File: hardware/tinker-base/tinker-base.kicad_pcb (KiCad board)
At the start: 4 copper layers, 30.3 x 90.5 mm, 86 parts, among them J2 TYPE-C-31-M-12, J8 CON-SMA-EDGE-S, Q1 FS8205A, Q2 FS8205A, Q3 FS8205A, U1 W25Q128JVYIQ, U14 DW01A, U15 AANI-CH-0070, U16 E220-900MM22S, U22 TPS22918DBVR, U3 ESP32-S3RH2, U5 BQ21040DBVR, U9 TPS63020DSJR, Y1 ABS07-32.768KHZ-T, Y2 ECS-400-10-37B2-CKY-TR

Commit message: hardware(Tinker-Base): V1 design review and fixes -- the antenna window clear on every layer, 21 ground vias, L5/C25/fiducials, R52 1.2 k, and fab notes for the order
Stacked on #1545 (the Beetle/Mantis parts). The V1 JLC package was plotted from
exactly this board (md5 1fe1e414).

The review is new: hardware/tinker-base/design-review-2026-09-28.md. It has a
table of the fixes applied, and of the items left undone with the reason for each.

Layout (tinker-base.kicad_pcb):
- U15 antenna. F.Cu keeps the feed notch. A second rule area clears In1, In2 and
  B.Cu under the whole 4.6 x 3.0 mm window. Before this, In1 GND, In2 +3V3 and
  B.Cu GND filled under the feed pads. Nine GND fence vias.
- 21 GND vias: nine beside signal vias (signal vias more than 1 mm from a
  ground via: 14 -> 5), nine in U3's exposed pad between its paste windows, one
  for C16/C24 and two for U16's ground pads. Five old vias removed.
- J8 moved so its pads start 0.30 mm inside the edge. L5 (330 nH) runs from the
  SMA line to GND beside it.
- C25 (100 nF) on V_SWITCH at U9.
- J2's signal pads trimmed to HRO's land, in the library too. BT2.P to J2 goes
  from 0.40 to 0.84 mm.
- S3 gets an F.Cu keep-out over its body, and its GPIO0 via moves out from
  under it.
- Thermal reliefs on J2's shell legs and D6's cathode. Pin-1 dots on U3, U5, U22,
  CR1 and U16. FID1-FID3 added, R13/R16 refs hidden, and a B.Silk "-" at BT2's
  N end.
- Zones refilled. A second kicad-cli refill reproduces them byte for byte.

Schematic:
- L5, C25 and FID1-FID3 added.
- R52 680 -> 1.2 k. The charge current drops from 0.79 A to about 0.45 A, so the
  charger's heat no longer trips the board-mounted NTC from room temperature.
- Title blocks, rev V1, on all four sheets.
- bom.csv regenerated.

Library:
- IC_ESP32-S3 and 8L_WSON_8x6x3p4x4p3_MAC go back to their window polygons.
  4078070b had added paste pads on top of those polygons.
- USB_C_HRO_TYPE-C-31-M-12 pads trimmed.
- ANT_AANI-CH-0070_ABR's description states the r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
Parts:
- added C25: 100 nF, Capacitor_SMD:C_0402_1005Metric, F.Cu at (48.9, 171.8)
- added FID1: Fiducial, Fiducial:Fiducial_0.5mm_Mask1mm, F.Cu at (53.9, 108.1)
- added FID2: Fiducial, Fiducial:Fiducial_0.5mm_Mask1mm, F.Cu at (74.4, 121.6)
- added FID3: Fiducial, Fiducial:Fiducial_0.5mm_Mask1mm, F.Cu at (51.4, 187.6)
- added L5: 330 nH, Inductor_SMD:L_0603_1608Metric, F.Cu at (62.1, 108.8)
- R52: value 680 -> 1.2 k
- moved J8 1.14 mm to (62.9, 105.7)
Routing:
- net Net-(U3-GPIO0): track 14.2 -> 11.8 mm
- net GND: track 2.66 -> 3.69 mm, vias 184 -> 210

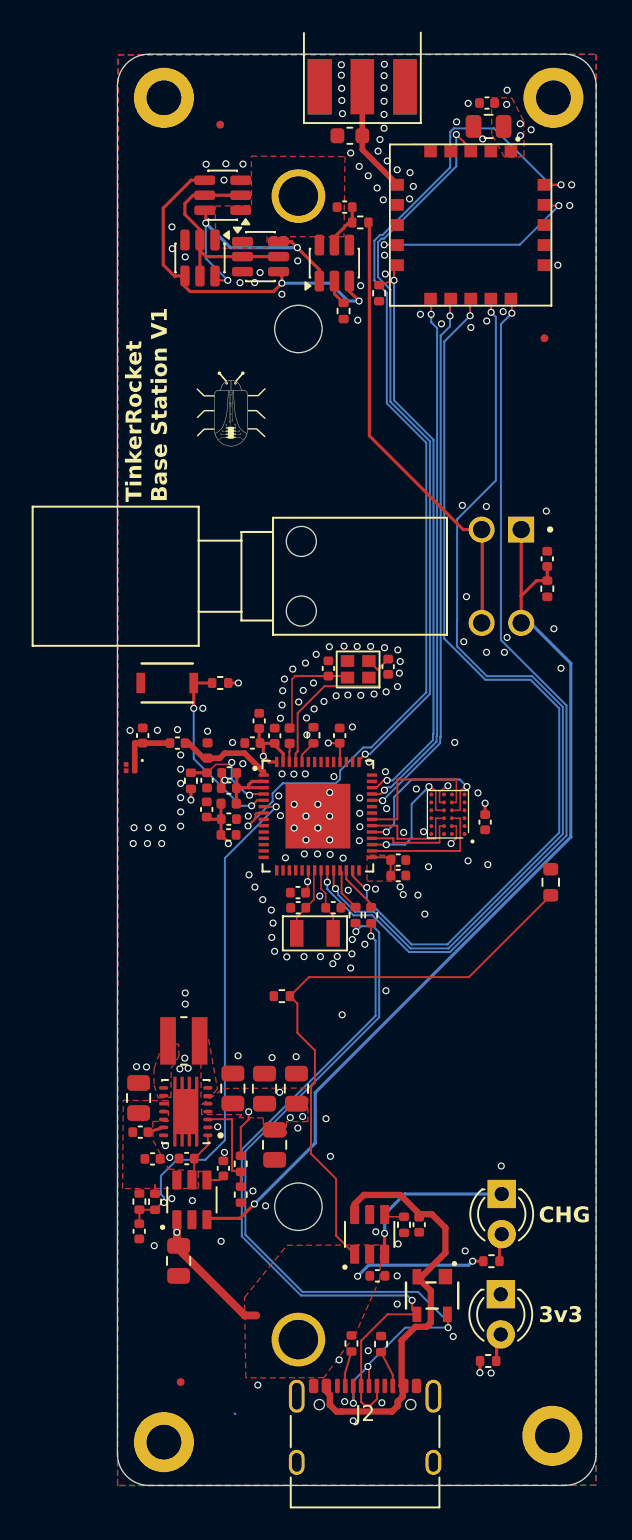
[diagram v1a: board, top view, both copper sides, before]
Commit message: hardware(Tinker-Base): three vias off their pads, and J2's rear fillets kept flat under BT2
Three vias had rings overlapping an SMD land. The first and third had their holes
at, or inside, the edge of the land's mask opening, so solder could wick down them.

- C16/C24 GND via, from (54.20, 149.55) to (53.52, 149.60). It sat in the 0.34 mm gap
  between C24.2 and C16.2. It now sits in the pocket between C8.1, C8.2, C24.2 and C16.2,
  with a 0.2 mm stub to the caps' strap, and serves C8.2 too. GPIO0's B.Cu diagonal,
  a static strap line, moves 0.5 mm down-right to free that pocket.
- U16 GND via, from (70.50, 109.00) on C20.1's edge to (70.97, 109.045). A 0.25 mm stub
  runs to U16 pad 2.
- U22 VCC via, from (51.16, 178.13) to (50.44, 178.25). It sat 0.19 mm below U22.1,
  inside that pad's 0.10 mm mask margin. It now sits beside the U22.1-C42.1 trace with a
  0.25 mm F.Cu stub. The In2 VCC track (µA) drops straight down to it.

Now no via ring touches any SMD mask opening except U3's nine thermal-pad vias. The
closest via hole is 0.10 mm from an opening, at C88.

BT2's flat base ends over the first 0.27 mm of J2's two rear shell-leg pads, which are
soldered from the bottom. The fab notes now say to keep those two fillets flat.

Checks:
- DRC (--severity-all --schematic-parity): 0 errors, the same 26 warnings, 0 unconnected,
  0 parity.
- The stored fills are a kicad-cli refill, and a second refill is byte-identical.
- check_board_parity: tinker-base 90/90.
- Signal vias more than 1 mm from a GND via: 5, unchanged.
- The U15 window is still clear. No footprint moved.

Co-Authored-By: Claude Opus 5.5 <noreply@anthropic.com>
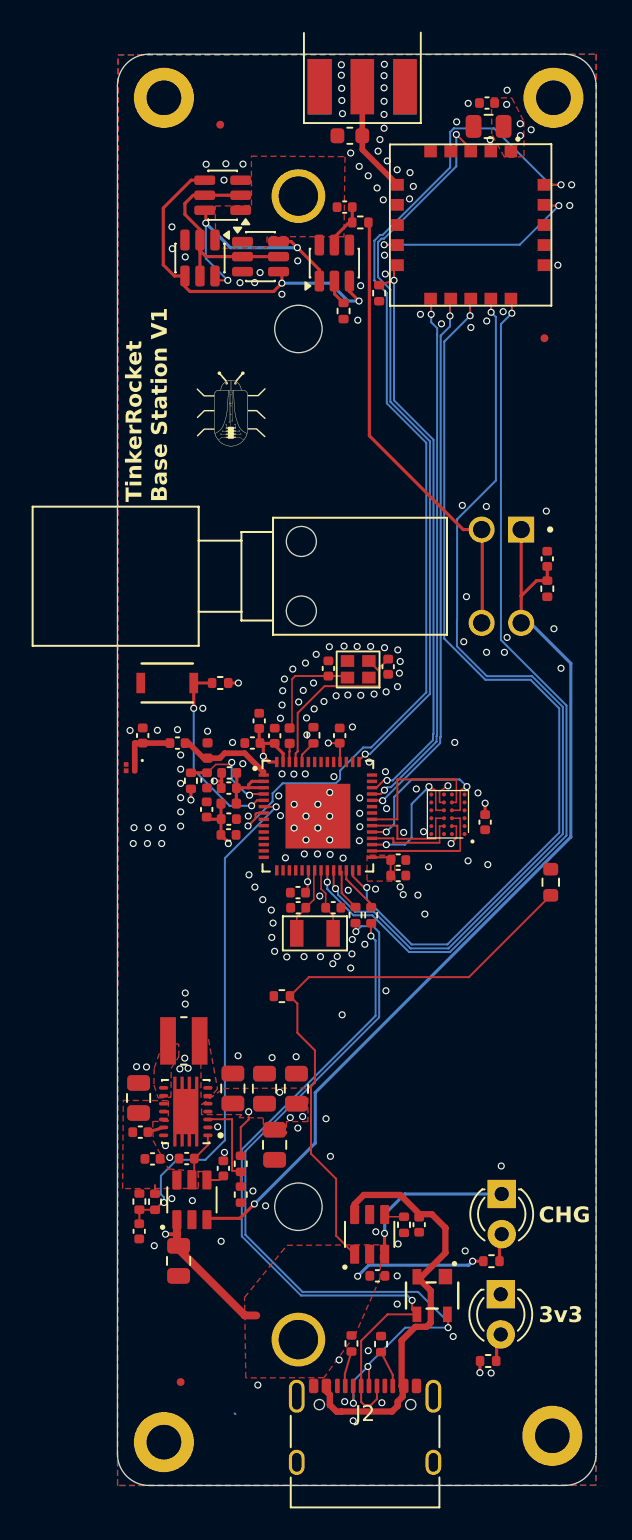
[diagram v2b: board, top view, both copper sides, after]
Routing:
- net GND: track 3.69 -> 4.91 mm
- net VCC: track 99.6 -> 100.1 mm
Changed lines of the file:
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@@
 	)
 	(segment
+		(start 70.97 109.045)
+		(end 71.01 109.79)
+		(width 0.25)
+		(layer "F.Cu")
+		(net "GND")
+	)
+	(segment
 		(start 60.53 142.06)
 		(end 60.52 142.05)
@@
 	)
 	(segment
-		(start 53.99 149.085)
+		(start 53.99 149.6)
 		(end 53.99 150.045)
 		(width 0.2)
@@
 		(net "GND")
 	)
+	(segment
+		(start 53.99 149.085)
+		(end 53.99 149.6)
+		(width 0.2)
+		(layer "F.Cu")
+		(net "GND")
+	)
+	(segment
+		(start 53.52 149.6)
+		(end 53.99 149.6)
+		(width 0.2)
+		(layer "F.Cu")
+		(net "GND")
+	)
 	(via
 		(at 65.5 152.85)
@@
 	)
 	(via
-		(at 54.2 149.55)
+		(at 53.52 149.6)
 		(size 0.45)
 		(drill 0.3)
@@
 	)
 	(via
-		(at 70.5 109)
+		(at 70.97 109.045)
 		(size 0.45)
 		(drill 0.3)
@@
 	)
 	(segment
-		(start 55.205 151.165)
+		(start 54.498 151.165)
 		(end 55.885 151.165)
 		(width 0.127)
@@
 	)
 	(segment
-		(start 52.226 148.186)
-		(end 55.205 151.165)
+		(start 52.226 148.893)
+		(end 54.498 151.165)
 		(width 0.127)
 		(layer "B.Cu")
@@
 	(segment
 		(start 52.226 145)
-		(end 52.226 148.186)
+		(end 52.226 148.893)
 		(width 0.127)
 		(layer "B.Cu")
@@
 	(segment
 		(start 51.16 177.335)
-		(end 51.16 178.13)
+		(end 51.16 178.25)
 		(width 0.5)
 		(layer "F.Cu")
@@
 	)
 	(segment
+		(start 50.44 178.25)
+		(end 51.16 178.25)
+		(width 0.25)
+		(layer "F.Cu")
+		(net "VCC")
+	)
+	(segment
 		(start 63.33 114.34)
 		(end 63.27 114.28)
@@
 	)
 	(segment
-		(start 51.16 178.13)
+		(start 51.16 178.25)
 		(end 51.16 178.62)
 		(width 0.5)
@@
 	)
 	(via
-		(at 51.16 178.13)
+		(at 50.44 178.25)
 		(size 0.45)
 		(drill 0.3)
@@
 	)
 	(segment
-		(start 51.16 178.13)
+		(start 50.44 178.25)
 		(end 50.44 177.41)
 		(width 0.5)

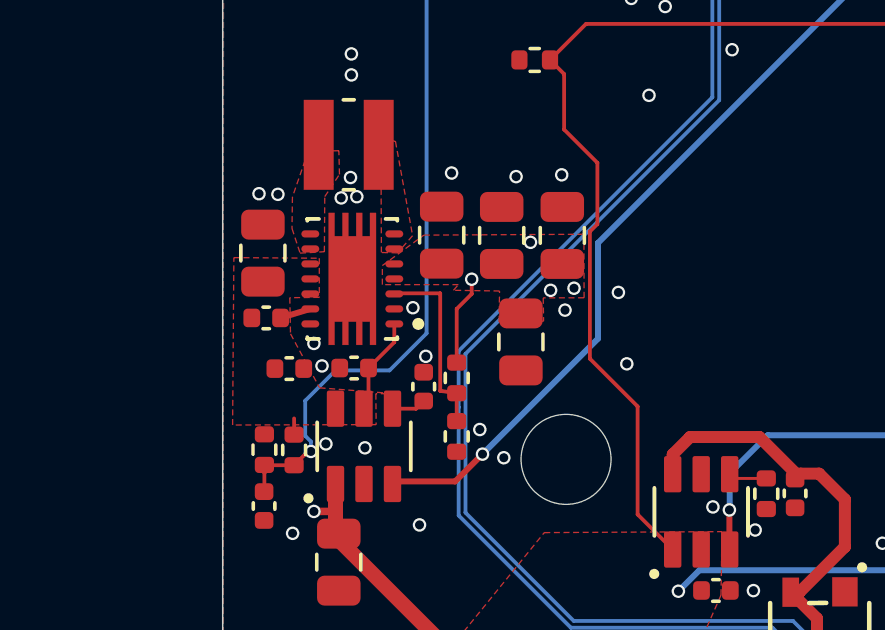
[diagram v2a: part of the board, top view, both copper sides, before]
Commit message: hardware(Tinker-Base): C26, 100 nF on U9's output beside VOUT, with FB running under it
Review item L8, output side, added at the owner's word. The 22 uF output caps'
ground pads return around the L2 switch-node pour, so the output had no short
high-frequency loop. C25 already fixes the same problem on the input side.

- C26: 100 nF, 0402, +3V3 to GND. It is drawn on the Power Switch sheet with
  #PWR0239/#PWR0240, and C23 was the template.
- Placement: (54.68, 171.48), rotated 180. The +3V3 pad sits on R13's +3V3 feed
  and on the output pour. That pour is the same top-layer copper as U9's VOUT
  pins and C58.
- FB: U9's FB line runs under the cap's body, between the pads, with 0.1265 mm
  and 0.1665 mm clearance. Its route is unchanged.
- Ground: U9 pin 2's GND via moves from (53.74, 171.46) to (53.77, 172.12), which
  C26's GND pad would otherwise have overlapped. A 0.25 mm link joins that pad to
  the via, which still serves pin 2 through the same top-layer ground.

Checks:
- DRC (--severity-all --schematic-parity): 0 errors, the same 26 warnings,
  0 unconnected, 0 parity.
- The stored fills are a kicad-cli refill, and a second refill is byte-identical.
- check_board_parity: tinker-base 91/91.
- ERC: 35 errors, unchanged.
- No via ring touches an SMD mask opening except U3's nine.
- The U15 window is still clear.
- bom.csv: C26 joins the 100 nF line, now 13. The generator reproduces the
  previous bom.csv exactly from the previous netlist.

Co-Authored-By: Claude Opus 5.5 <noreply@anthropic.com>
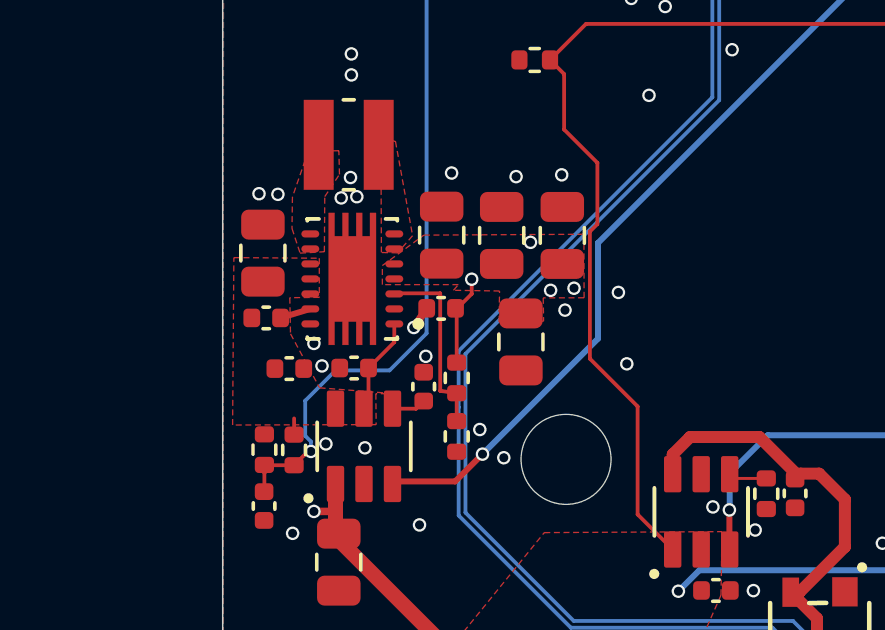
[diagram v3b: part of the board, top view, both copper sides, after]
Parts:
- added C26: 100 nF, Capacitor_SMD:C_0402_1005Metric, F.Cu at (54.7, 171.5)
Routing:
- net GND: track 4.91 -> 5.68 mm
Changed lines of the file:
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@@
+		)
+	)
+	(footprint "Capacitor_SMD:C_0402_1005Metric"
+		(layer "F.Cu")
+		(at 54.68 171.48 180)
+		(descr "Capacitor SMD 0402 (1005 Metric), square (rectangular) end terminal, IPC-7351 nominal, (Body size source: IPC-SM-782 page 76, https://www.pcb-3d.com/wordpress/wp-content/uploads/ipc-sm-782a_amendment_1_and_2.pdf)")
+		(tags "capacitor")
+		(property "Reference" "C26"
+			(at 0 -1.16 180)
+			(layer "F.SilkS")
+			(hide yes)
+			(effects
+				(font
+					(size 1 1)
+					(thickness 0.15)
+				)
+			)
+		)
+		(property "Value" "100 nF"
+			(at 0 1.16 180)
+			(layer "F.Fab")
+			(hide yes)
+			(effects
+				(font
+					(size 1 1)
+					(thickness 0.15)
+				)
+			)
+		)
+		(property "Datasheet" ""
+			(at 0 0 180)
+			(layer "F.Fab")
+			(hide yes)
+			(effects
+				(font
+					(size 1.27 1.27)
+				)
+			)
+		)
+		(property "Description" ""
+			(at 0 0 180)
+			(layer "F.Fab")
+			(hide yes)
+			(effects
+				(font
+					(size 1.27 1.27)
+				)
+			)
+		)
+		(property "KiLib_Generator" "SMD_2terminal_chip_molded"
+			(at 0 0 180)
+			(layer "F.SilkS")
+			(hide yes)
+			(effects
+				(font
+					(size 1 1)
+					(thickness 0.15)
+				)
+			)
+		)
+		(property "MPN" "CL05B104KO5NNNC"
+			(at 0 0 180)
+			(unlocked yes)
+			(layer "F.Fab")
+			(hide yes)
+			(effects
+				(font
+					(size 1 1)
+					(thickness 0.15)
+				)
+			)
+		)
+		(property "Mfr" "Samsung"
+			(at 0 0 180)
+			(unlocked yes)
+			(layer "F.Fab")
+			(hide yes)
+			(effects
+				(font
+					(size 1 1)
+					(thickness 0.15)
+				)
+			)
+		)
+		(sheetname "/Power Switch/")
+		(sheetfile "power.kicad_sch")
+		(attr smd)
+		(duplicate_pad_numbers_are_jumpers no)
+		(fp_line
+			(start -0.107836 0.36)
+			(end 0.107836 0.36)
+			(stroke
+				(width 0.12)
+				(type solid)
+			)
+			(layer "F.SilkS")
+		)
+		(fp_line
+			(start -0.107836 -0.36)
+			(end 0.107836 -0.36)
+			(stroke
+				(width 0.12)
+				(type solid)
+			)
+			(layer "F.SilkS")
+		)
+		(fp_rect
+			(start -0.91 -0.46)
+			(end 0.91 0.46)
+			(stroke
+				(width 0.05)
+				(type solid)
+			)
+			(fill no)
+			(layer "F.CrtYd")
+		)
+		(fp_rect
+			(start -0.5 -0.25)
+			(end 0.5 0.25)
+			(stroke
+				(width 0.1)
+				(type solid)
+			)
+			(fill no)
+			(layer "F.Fab")
+		)
+		(fp_text user "${REFERENCE}"
+			(at 0 0 0)
+			(layer "F.Fab")
+			(effects
+				(font
+					(size 0.25 0.25)
+					(thickness 0.04)
+				)
+			)
+		)
+		(pad "1" smd roundrect
+			(at -0.48 0 180)
+			(size 0.56 0.62)
+			(layers "F.Cu" "F.Mask" "F.Paste")
+			(roundrect_rratio 0.25)
+			(net "+3V3")
+			(pintype "passive")
+		)
+		(pad "2" smd roundrect
+			(at 0.48 0 180)
+			(size 0.56 0.62)
+			(layers "F.Cu" "F.Mask" "F.Paste")
+			(roundrect_rratio 0.25)
+			(net "GND")
+			(pintype "passive")
+		)
+		(embedded_fonts no)
+		(model "${KICAD10_3DMODEL_DIR}/Capacitor_SMD.3dshapes/C_0402_1005Metric.step"
+			(offset
+				(xyz 0 0 0)
+			)
+			(scale
+				(xyz 1 1 1)
+			)
+			(rotate
+				(xyz 0 0 0)
+			)
 		)
 	)
@@
 	)
 	(segment
+		(start 54.2 171.48)
+		(end 53.77 172.12)
+		(width 0.25)
+		(layer "F.Cu")
+		(net "GND")
+	)
+	(segment
 		(start 53.99 149.6)
 		(end 53.99 150.045)
@@
 	)
 	(via
-		(at 53.74 171.46)
+		(at 53.77 172.12)
 		(size 0.45)
 		(drill 0.3)
